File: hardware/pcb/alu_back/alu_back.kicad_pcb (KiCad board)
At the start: 2 copper layers, 9 parts, among them J1 Conn_01x04_Female, U1 Register A, U2 Register B, U3 Register C, U4 Register D, U5 Add/Sub, U6 And/Or, U7 Xor/Not, U8 Shift

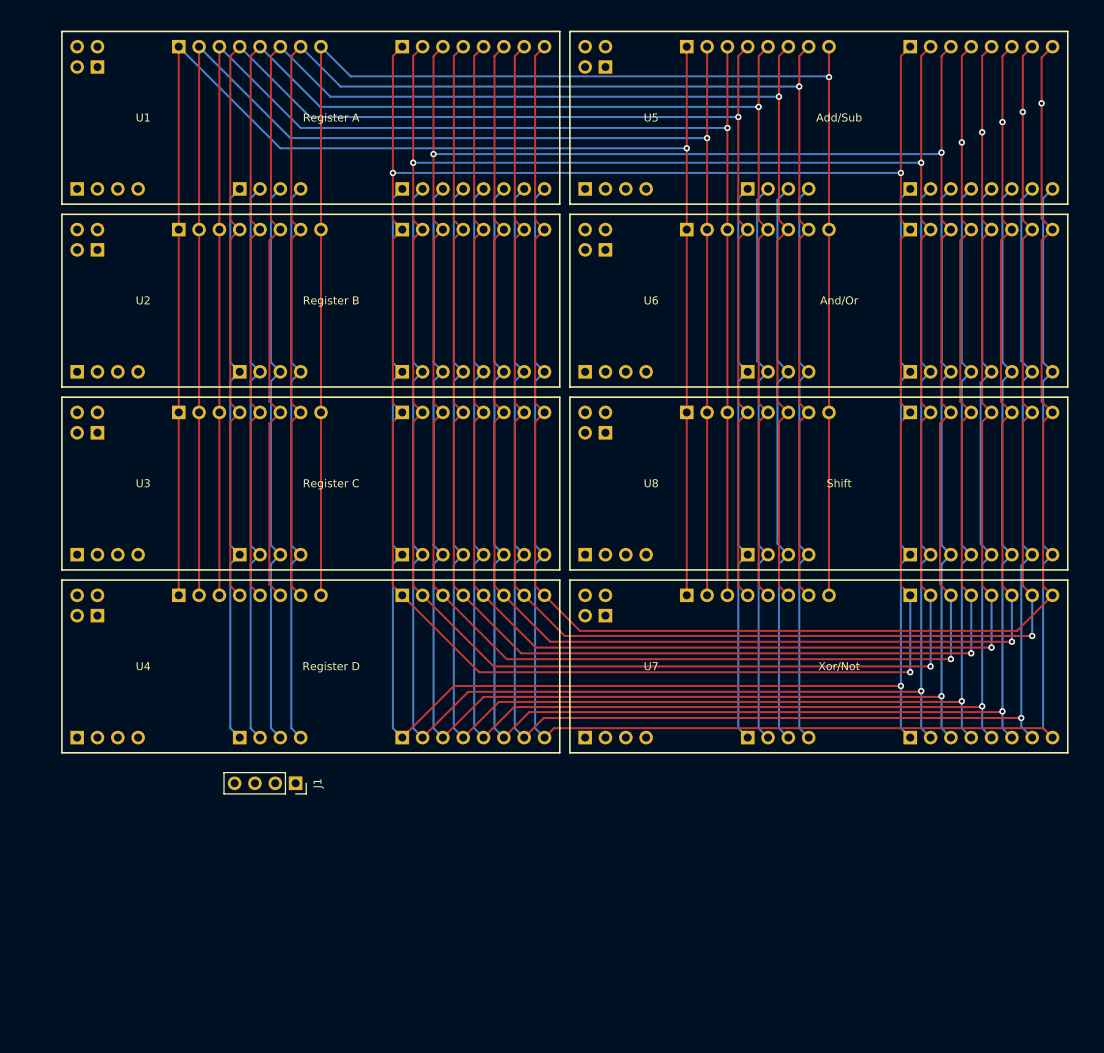
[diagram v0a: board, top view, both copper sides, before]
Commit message: Board routing and fills
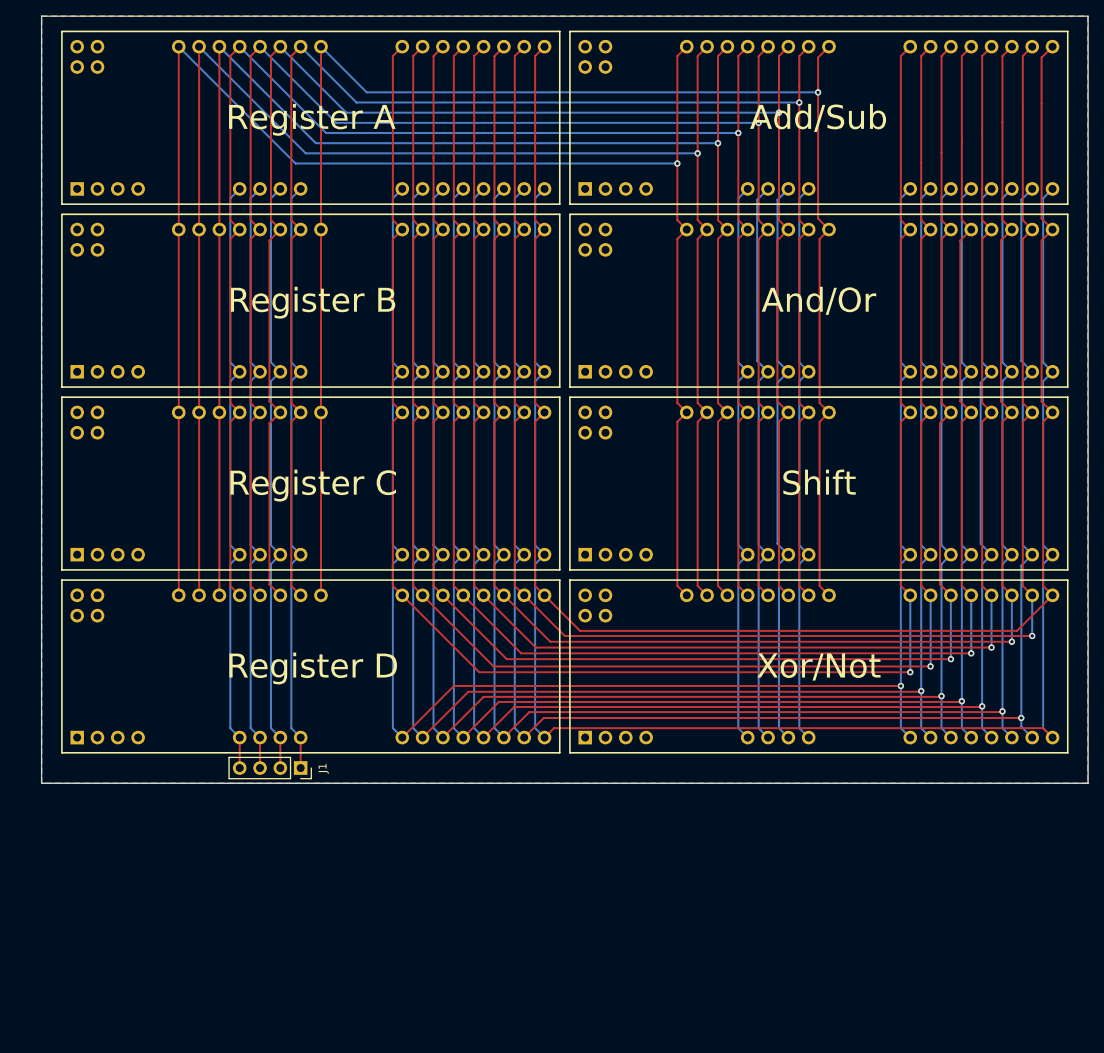
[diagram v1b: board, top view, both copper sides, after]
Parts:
- moved J1 2.01 mm to (57.8, 117.5)
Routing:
- net /A5: track 281.5 -> 217.9 mm, vias 3 -> 1
- net /A6: track 282.6 -> 219.1 mm, vias 3 -> 1
- net /A7: track 283.6 -> 220.1 mm, vias 3 -> 1
- net ~RESET~: track 71.5 -> 75.3 mm
- net ~CLK~: track 71.5 -> 75.3 mm
- net RESET: track 71.5 -> 75.3 mm
- net CLK: track 71.5 -> 75.3 mm
- net /BUS6: track 205.4 -> 207.9 mm
- net /BUS7: track 205.9 -> 208.5 mm
- net /BUS5: track 204.9 -> 207.4 mm
- net /BUS0: track 202.2 -> 204.7 mm
- net /BUS3: track 208.4 -> 209.3 mm
- net /BUS4: track 209.0 -> 209.8 mm
- net /BUS2: track 208.4 -> 209.2 mm
- net /BUS1: track 207.4 -> 208.2 mm
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- added copper zone on B.Cu, net GND
- added copper zone on F.Cu, net VCC
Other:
- board outline added: 130.8 x 95.9 mm

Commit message: Flags board
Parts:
- added U9: Flags, CPU_Modules:Flags_board, F.Cu at (27.9, 116.8)
- moved J1 24.1 mm to (57.8, 141.6)
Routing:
- net /CAF: track 71.8 -> 106.9 mm
- net /Z: track 71.5 -> 106.6 mm
- net /V: track 71.7 -> 106.8 mm
- net /CFA: track 71.5 -> 106.6 mm
- net ~RESET~: track 75.3 -> 100.6 mm
- net ~CLK~: track 75.3 -> 100.4 mm
- net CLK: track 75.3 -> 100.4 mm
- net RESET: track 75.3 -> 100.4 mm
- net /BUS2: track 209.2 -> 233.2 mm
- net /BUS4: track 209.8 -> 233.6 mm
- net /BUS3: track 209.3 -> 233.1 mm
- net /BUS1: track 208.2 -> 232.1 mm
- net /BUS6: track 207.9 -> 230.8 mm
- net /BUS7: track 208.5 -> 231.3 mm
- net /BUS5: track 207.4 -> 230.3 mm
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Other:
- board size 130.8 x 95.9 mm -> 130.8 x 127.6 mm

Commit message: Add some connectors
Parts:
- added J2: BUS, Connector_PinSocket_2.54mm:PinSocket_1x08_P2.54mm_Vertical, F.Cu at (106.0, 121.3)
- added J3: FLAGS, Connector_PinSocket_2.54mm:PinSocket_1x04_P2.54mm_Vertical, F.Cu at (92.7, 121.3)
- J1: value Conn_01x04_Female -> SYNC
- moved J1 57.4 mm to (113.7, 128.3)
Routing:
- net ~RESET~: track 100.6 -> 154.8 mm
- net CLK: track 100.4 -> 154.6 mm
- net RESET: track 100.4 -> 154.6 mm
- net ~CLK~: track 100.4 -> 154.6 mm
- net /BUS4: track 233.6 -> 260.0 mm
- net /BUS3: track 233.1 -> 259.5 mm
- net /BUS2: track 233.2 -> 259.6 mm
- net /BUS1: track 232.1 -> 258.4 mm
- net /BUS6: track 230.8 -> 256.2 mm
- net /BUS0: track 227.6 -> 253.0 mm
- net /BUS7: track 231.3 -> 256.7 mm
- net /BUS5: track 230.3 -> 255.7 mm
- net Net-(J3-Pad3): track 0.00 -> 20.2 mm
- net Net-(J3-Pad4): track 0.00 -> 20.2 mm
- net Net-(J3-Pad2): track 0.00 -> 20.2 mm
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
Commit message: ALU backplane board
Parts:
- added C1: 10uF, Capacitor_SMD:C_0805_2012Metric_Pad1.18x1.45mm_HandSolder, F.Cu at (134.6, 134.9)
- added C2: 100nF, Capacitor_SMD:C_0805_2012Metric_Pad1.18x1.45mm_HandSolder, F.Cu at (39.1, 110.2)
- added C3: 100nF, Capacitor_SMD:C_0805_2012Metric_Pad1.18x1.45mm_HandSolder, F.Cu at (39.1, 65.0)
- added C4: 100nF, Capacitor_SMD:C_0805_2012Metric_Pad1.18x1.45mm_HandSolder, F.Cu at (97.0, 65.0)
- added C5: 100nF, Capacitor_SMD:C_0805_2012Metric_Pad1.18x1.45mm_HandSolder, F.Cu at (135.6, 119.4)
- added H1: MountingHole, MountingHole:MountingHole_3mm, F.Cu at (35.6, 36.2)
- added H2: MountingHole, MountingHole:MountingHole_3mm, F.Cu at (43.2, 132.1)
- added H3: MountingHole, MountingHole:MountingHole_3mm, F.Cu at (148.6, 134.0)
- added H4: MountingHole, MountingHole:MountingHole_3mm, F.Cu at (128.9, 30.5)
- added H5: MountingHole, MountingHole:MountingHole_3mm, F.Cu at (95.2, 81.9)
- added J4: OUT, Connector_PinSocket_2.54mm:PinSocket_1x08_P2.54mm_Vertical, F.Cu at (24.8, 34.9)
- added J5: FCTL, Connector_PinSocket_2.54mm:PinSocket_1x04_P2.54mm_Vertical, F.Cu at (24.8, 136.5)
- added J6: LOAD, Connector_PinSocket_2.54mm:PinSocket_1x04_P2.54mm_Vertical, F.Cu at (24.8, 60.3)
- added J7: ARGS, Connector_PinSocket_2.54mm:PinSocket_1x08_P2.54mm_Vertical, F.Cu at (24.8, 83.2)
- added J8: POWER, Connector_PinSocket_2.54mm:PinSocket_2x02_P2.54mm_Vertical, F.Cu at (137.8, 136.5)
- added U10: 74HC125, Package_SO:SO-14_3.9x8.65mm_P1.27mm, F.Cu at (98.4, 59.4)
- added U11: 74HC245, Package_SO:SO-20_12.8x7.5mm_P1.27mm, F.Cu at (143.5, 123.2)
- added U12: 74HC138, Package_SO:SO-16_3.9x9.9mm_P1.27mm, F.Cu at (35.6, 105.4)
- added U13: 74HC138, Package_SO:SO-16_3.9x9.9mm_P1.27mm, F.Cu at (35.6, 60.3)
- U8: value Shift -> Shift/Swap
- moved J1 90.1 mm to (24.8, 113.7), turned to 0 degrees
- moved J3 15.3 mm to (93.3, 136.5)
- moved J2 15.2 mm to (106.0, 136.5)
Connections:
- U1 pad 1: Net-(U1-Pad1) -> OUT_A
- U1 pad 2: Net-(U1-Pad2) -> LOAD_A
- U1 pad 3: Net-(U1-Pad3) -> ARG_AA
- U1 pad 4: Net-(U1-Pad4) -> ARG_AB
- U2 pad 1: Net-(U2-Pad1) -> OUT_B
- U2 pad 2: Net-(U2-Pad2) -> LOAD_B
- U2 pad 3: Net-(U2-Pad3) -> ARG_BA
- U2 pad 4: Net-(U2-Pad4) -> ARG_BB
- U3 pad 1: Net-(U3-Pad1) -> OUT_C
- U3 pad 2: Net-(U3-Pad2) -> LOAD_C
- U3 pad 3: Net-(U3-Pad3) -> ARG_CA
- U3 pad 4: Net-(U3-Pad4) -> ARG_CB
- U4 pad 1: Net-(U4-Pad1) -> OUT_D
- U4 pad 2: Net-(U4-Pad2) -> LOAD_D
- U4 pad 3: Net-(U4-Pad3) -> ARG_DA
- U4 pad 4: Net-(U4-Pad4) -> ARG_DB
- U5 pad 1: Net-(U5-Pad1) -> OUT_AS
- U5 pad 2: Net-(U5-Pad2) -> ALT_AS
- U6 pad 1: Net-(U6-Pad1) -> OUT_AO
- U6 pad 2: Net-(U6-Pad2) -> ALT_AO
- U7 pad 1: Net-(U7-Pad1) -> OUT_XN
- U7 pad 2: Net-(U7-Pad2) -> ALT_XN
- U8 pad 1: Net-(U8-Pad1) -> OUT_S
- U8 pad 2: Net-(U8-Pad2) -> ALT_S
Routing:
- net ARG_B2: track 0.00 -> 181.3 mm, vias 0 -> 3
- net ALT: track 0.00 -> 156.9 mm, vias 0 -> 4
- net OUT_XN: track 0.00 -> 142.7 mm
- net OUT_S: track 0.00 -> 118.5 mm
- net OUT_AO: track 0.00 -> 94.9 mm
- net OUT_D: track 0.00 -> 73.2 mm
- net OUT_AS: track 0.00 -> 70.9 mm
- net ARG_AB: track 0.00 -> 65.5 mm
- net ARG_DA: track 0.00 -> 59.0 mm
- net ALT_XN: track 0.00 -> 56.7 mm, vias 0 -> 1
- net OUT_C: track 0.00 -> 52.9 mm
- net GND: track 0.00 -> 51.8 mm, vias 0 -> 11
- net LOAD_D: track 0.00 -> 49.8 mm, vias 0 -> 1
- net ARG_B0: track 0.00 -> 44.4 mm, vias 0 -> 1
- net ARG_B1: track 0.00 -> 42.0 mm, vias 0 -> 1
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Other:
- board size 130.8 x 127.6 mm -> 132.1 x 114.3 mm
- board text added: "+"
- board text added: "-"

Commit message: Backplane finishing touches
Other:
- board text added: "ALU Backplane v1.0"
- board text added: "JLCJLCJLCJLC"
- board text added: "Velko 2021"
